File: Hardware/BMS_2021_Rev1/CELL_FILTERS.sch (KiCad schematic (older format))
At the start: 46 parts

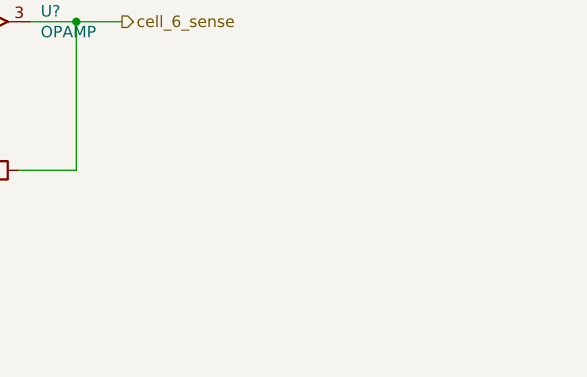
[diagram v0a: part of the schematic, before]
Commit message: TIVA added, current sense WIP
started the current sense circuit. added the tiva layout, need to ask if there is a better way
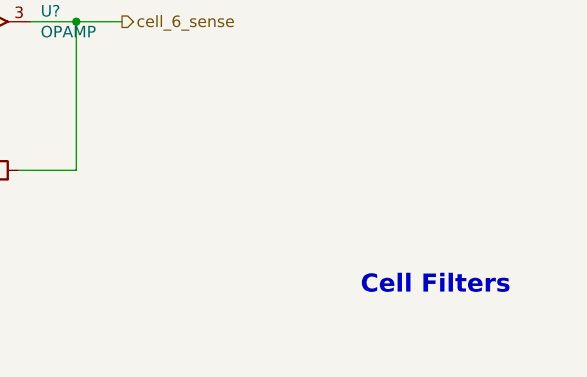
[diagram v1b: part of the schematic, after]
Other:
- note added: "Cell Filters"
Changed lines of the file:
@@
 $Descr USLetter 11000 8500
 encoding utf-8
-Sheet 3 3
+Sheet 3 4
 Title ""
 Date ""
@@
 Text Notes 7150 5550 0    50   Italic 10
 Questions: \nDiodes?\n
+Text Notes 7400 7750 2    79   ~ 16
+Cell Filters
 $EndSCHEMATC

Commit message: done (need to do LEDs)
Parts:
- removed R? (x13): R, symbol Device:R
- added R? (x13): 6.34M, symbol Device:R
- R?: value R -> 6.34M
- R?: value R -> 36.5k
- R?: value R -> 10k
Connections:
- net GND: now also R?.1, R?.1, R?.1, R?.1, R?.1, R?.1, R?.1
- net cell_3_sense: now also R?.1
- net cell_4_sense: now also R?.1
- net cell_5_sense: now also R?.1
- net cell_6_sense: now also R?.1
- net cell_7_sense: now also R?.1
- net cell_8_sense: now also R?.1
- net at R?.1, U?.1 (+): now also R?.2 (x6)
- net at R?.2, U?.2 (-): now also R?.2 (x5)
- net at R?.1, U?.2 (-): now also R?.2
- net at R?.2, U?.1 (+): now also R?.2
- net +5V renamed 5V

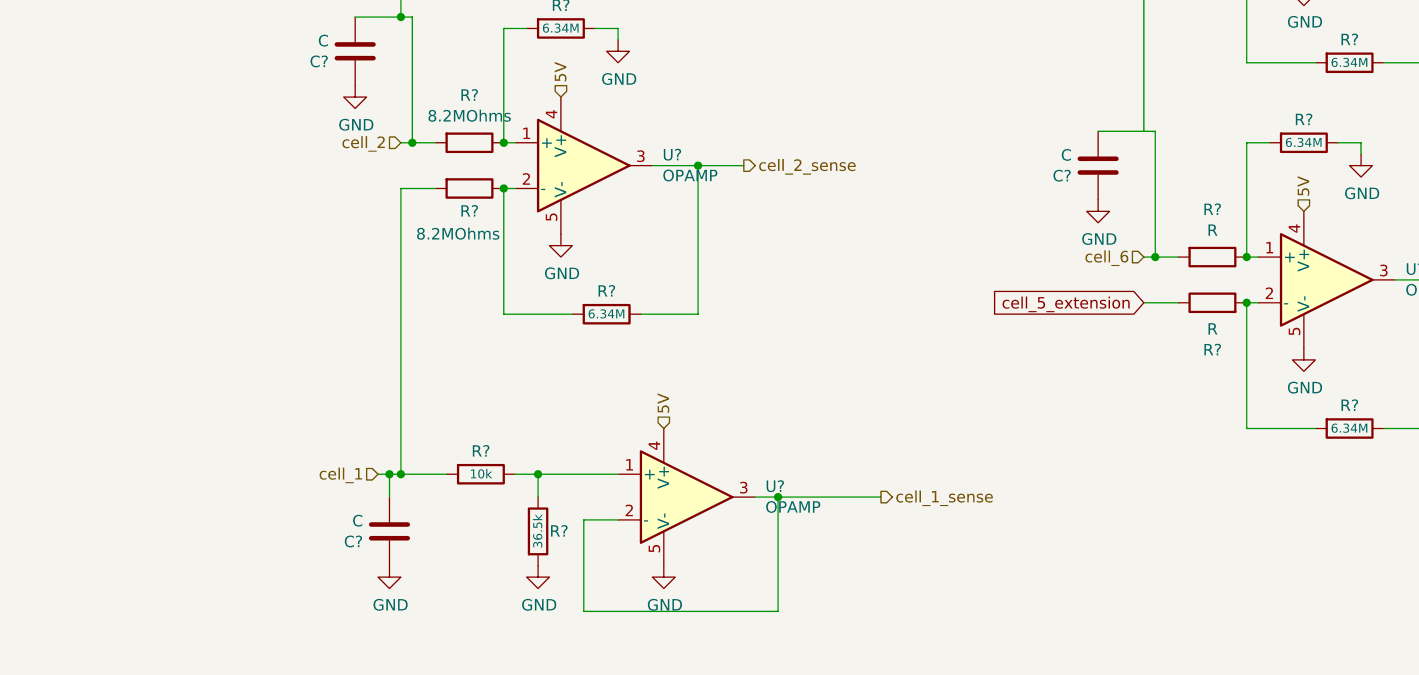
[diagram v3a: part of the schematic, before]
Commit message: notes from PDR made. to be fixed
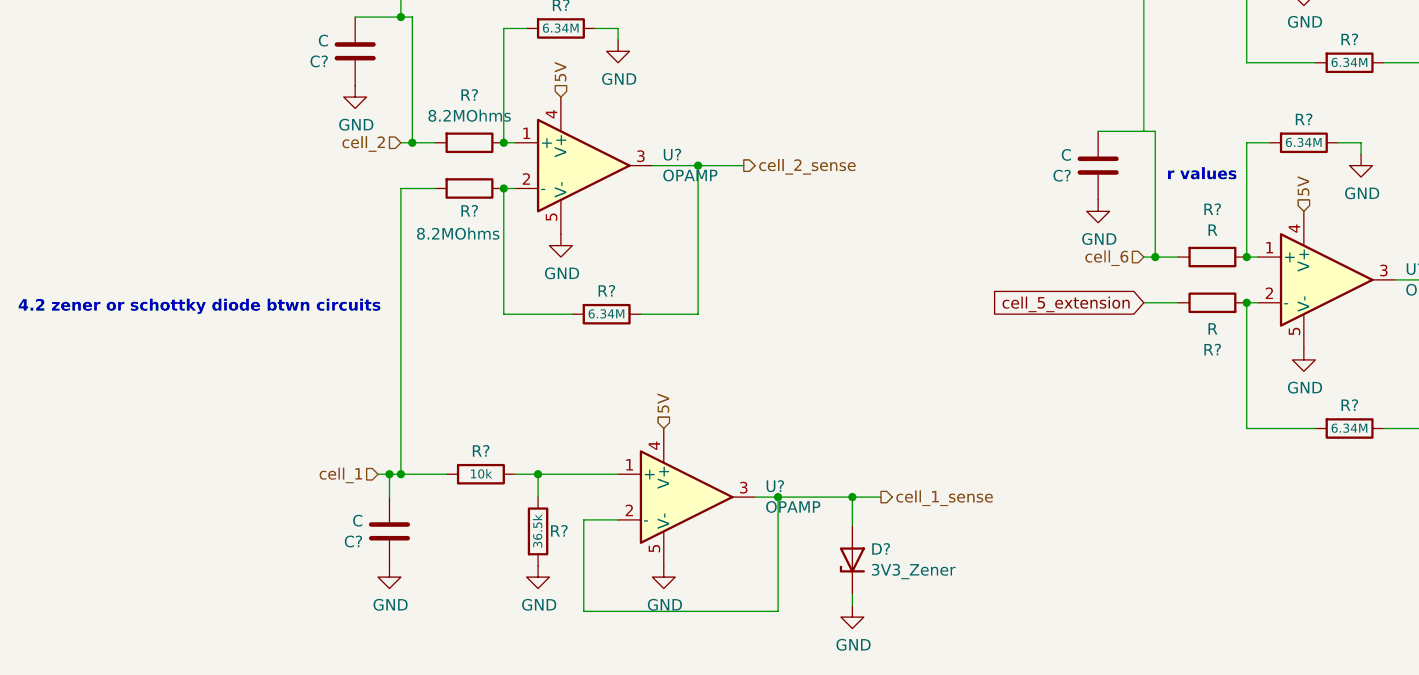
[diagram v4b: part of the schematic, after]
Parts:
- added D?: 3V3_Zener, symbol Device:D_Zener
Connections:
- net GND: now also D?.1 (K)
- net cell_1_sense: now also D?.2 (A)
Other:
- note added: "4.2 zener or schottky diode btwn circuits\n"
- note added: "r values"
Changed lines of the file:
@@
 	2600 7500 2500 7500
 Wire Wire Line
-	2600 7500 3050 7500
+	2600 7500 2925 7500
 Connection ~ 2600 7500
 $Comp
@@
 	0    1    1    0
 $EndComp
+$Comp
+L Device:D_Zener D?
+U 1 1 5F8CA6CA
+P 2925 7775
+F 0 "D?" V 2971 7695 50  0000 R CNN
+F 1 "3V3_Zener" V 2880 7695 50  0000 R CNN
+F 2 "" H 2925 7775 50  0001 C CNN
+F 3 "~" H 2925 7775 50  0001 C CNN
+	1    2925 7775
+	0    -1   -1   0
+$EndComp
+Wire Wire Line
+	2925 7625 2925 7500
+Connection ~ 2925 7500
+Wire Wire Line
+	2925 7500 3050 7500
+$Comp
+L power:GND #PWR?
+U 1 1 5F8D157C
+P 2925 7975
+F 0 "#PWR?" H 2925 7725 50  0001 C CNN
+F 1 "GND" H 2930 7802 50  0000 C CNN
+F 2 "" H 2925 7975 50  0001 C CNN
+F 3 "" H 2925 7975 50  0001 C CNN
+	1    2925 7975
+	1    0    0    -1
+$EndComp
+Wire Wire Line
+	2925 7975 2925 7925
+Text Notes -725 6700 0    50   ~ 10
+4.2 zener or schottky diode btwn circuits\n
+Text Notes 4300 6125 0    50   ~ 10
+r values
 $EndSCHEMATC

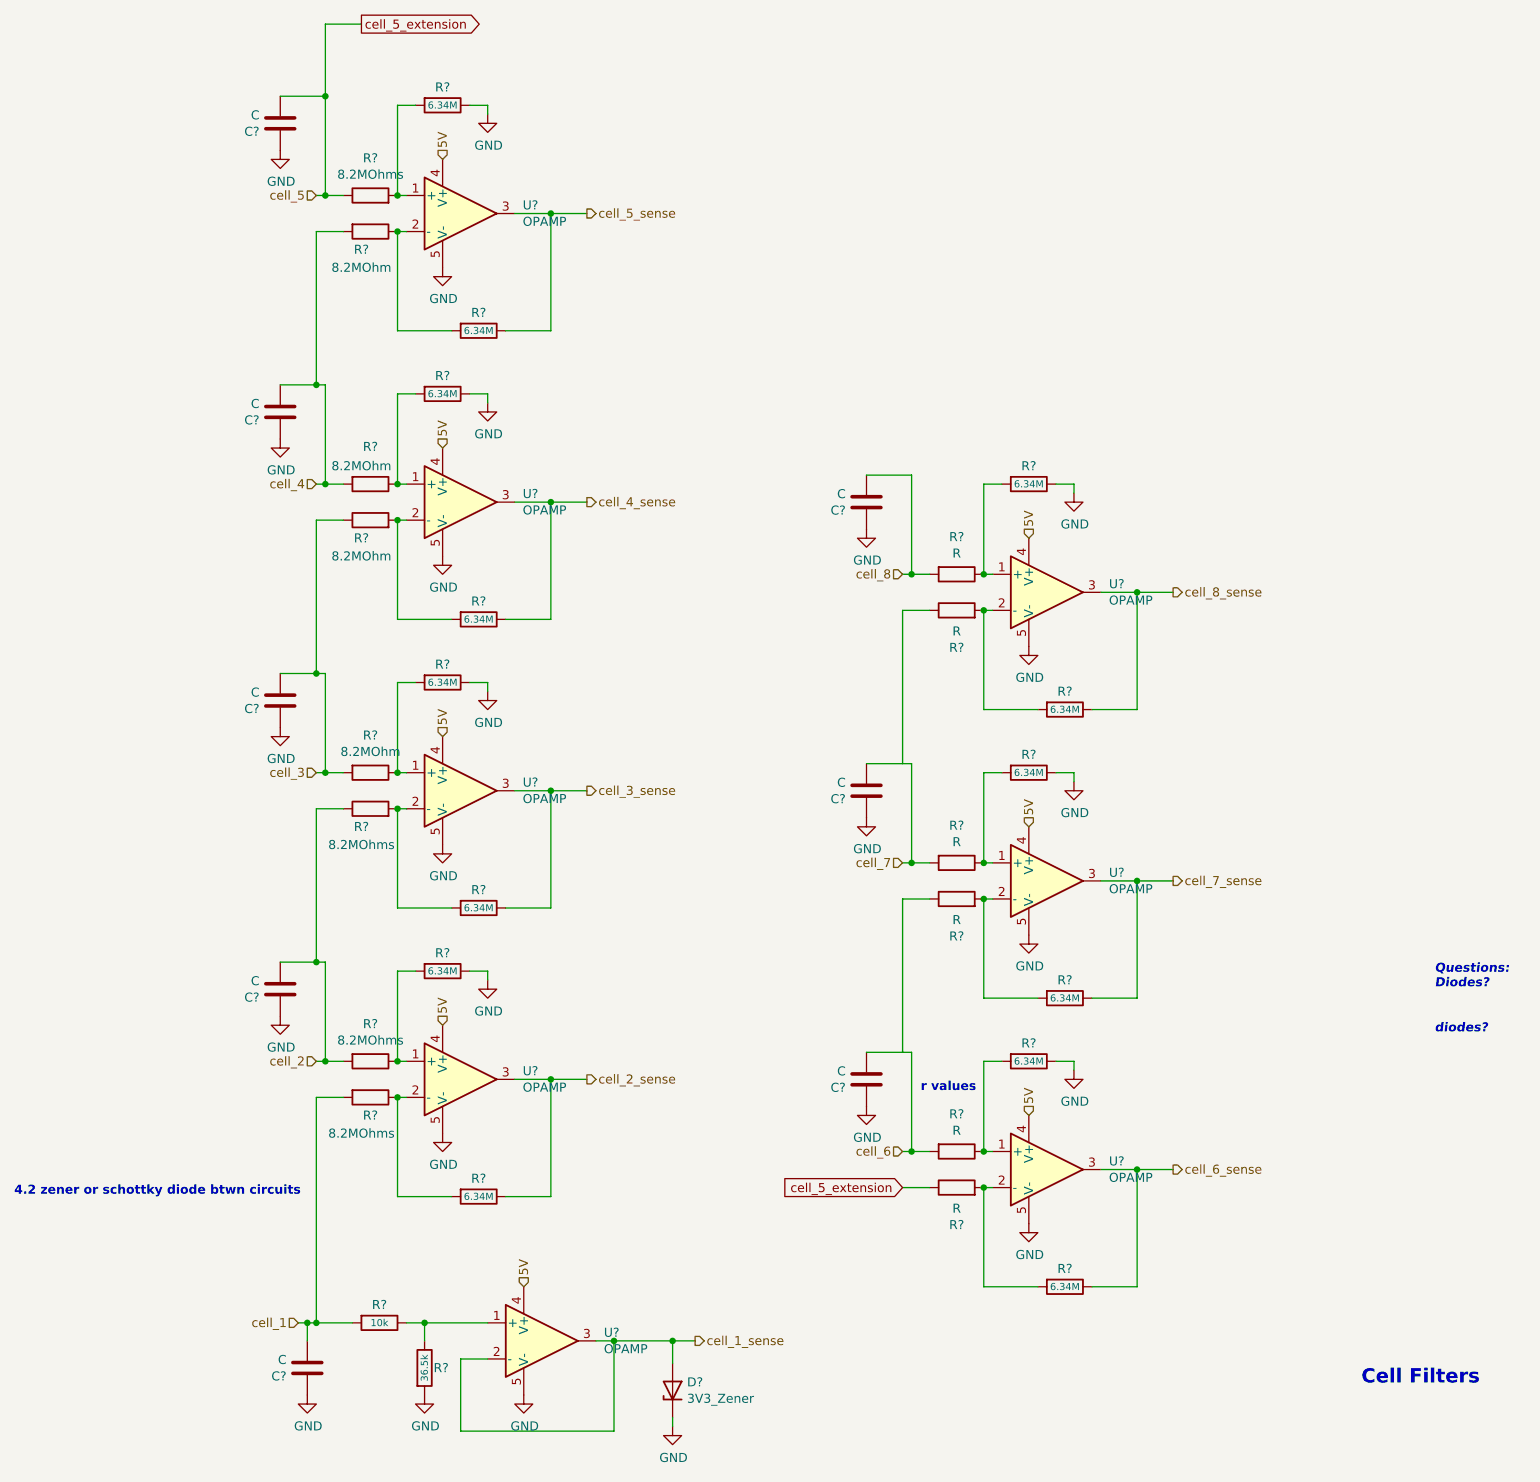
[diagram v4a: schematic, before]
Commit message: heirarchical sheets connected. Scho. diodes added to cell filters
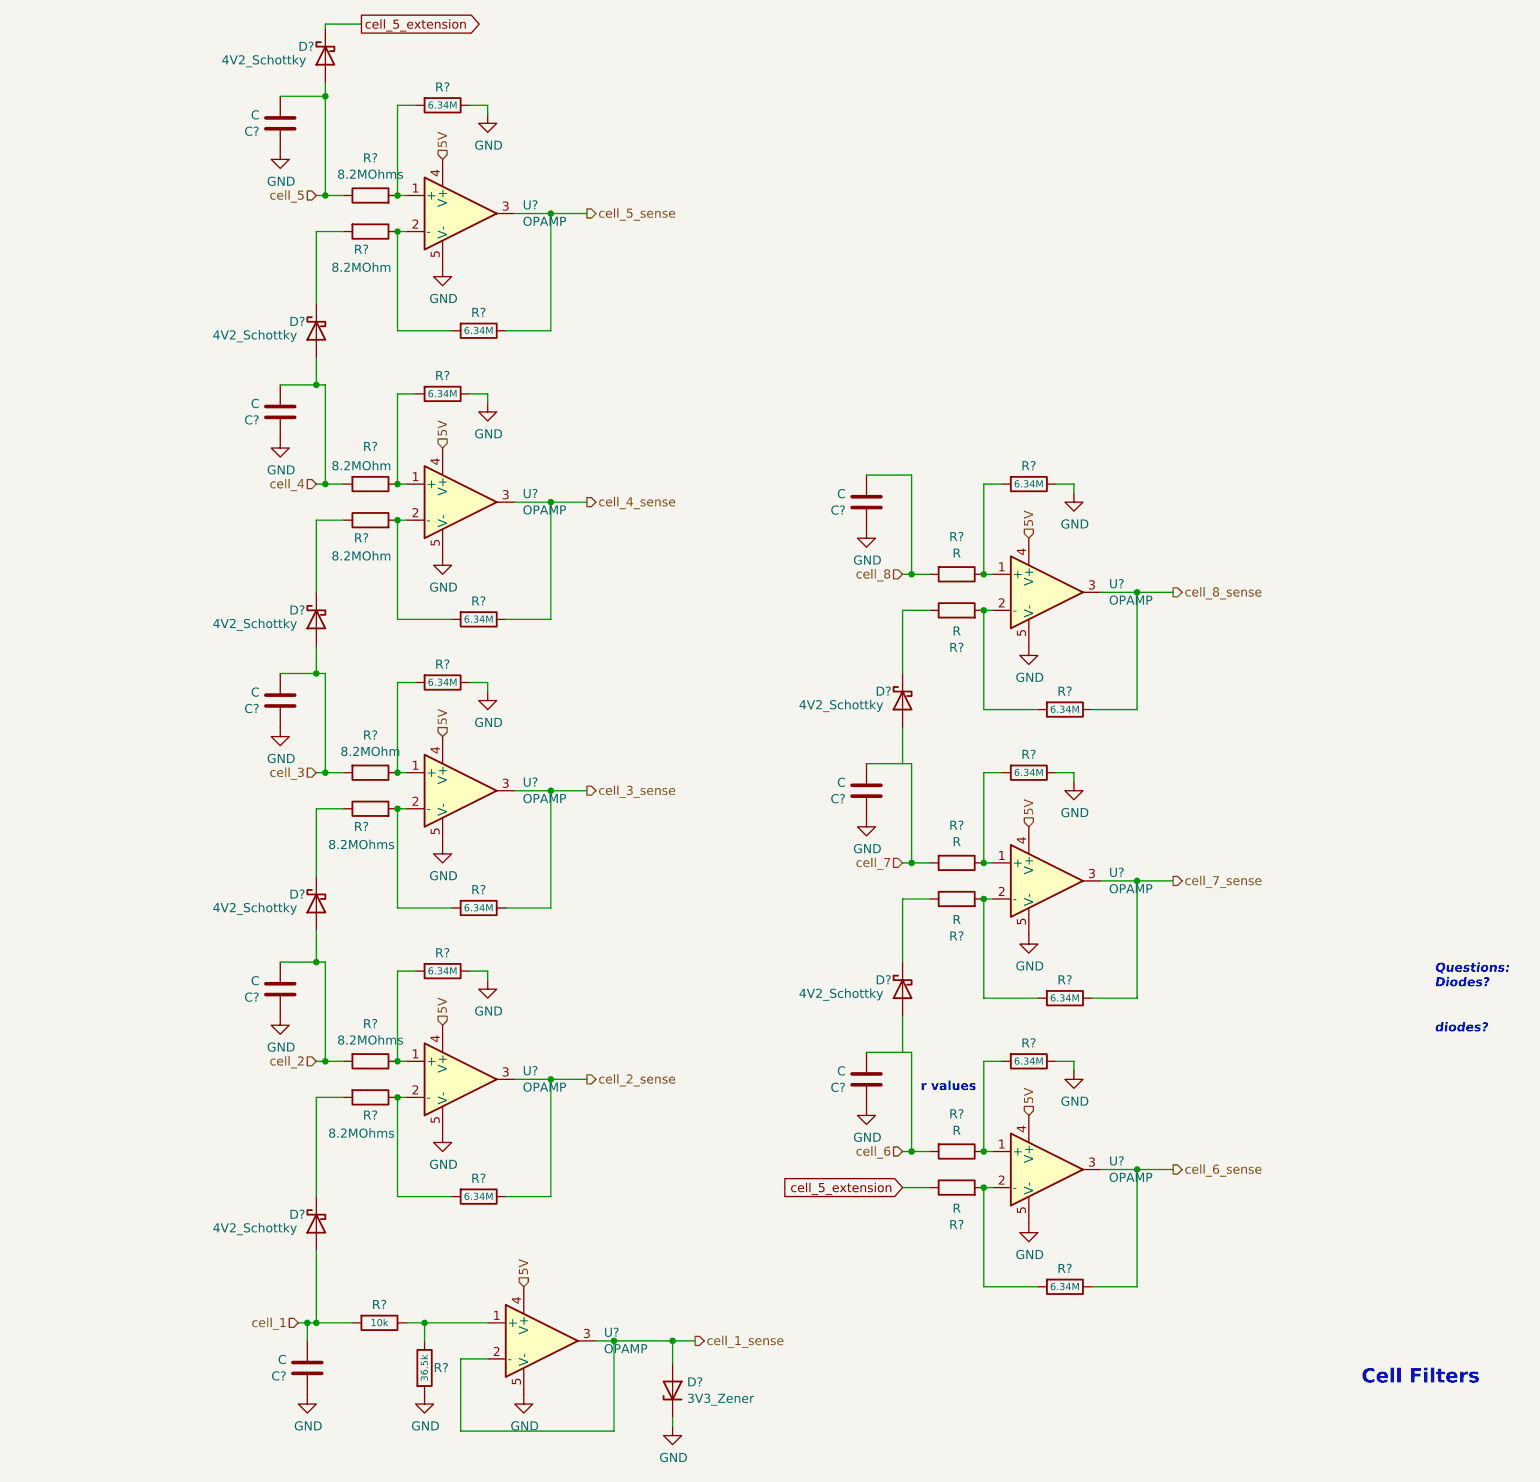
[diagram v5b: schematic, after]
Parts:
- added D? (x7): 4V2_Schottky, symbol Device:D_Schottky
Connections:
- net cell_1: now also D?.2 (A); no longer R?.2
- net cell_2: now also D?.2 (A); no longer R?.1
- net cell_3: now also D?.2 (A); no longer R?.1
- net cell_4: now also D?.2 (A); no longer R?.2
- net cell_5_extension: now also D?.1 (K); no longer C?.2, R?.1
- net at R?.1: now also D?.1 (K) (x2)
- new net: D?.1 (K), R?.2 (x2)
- new net: D?.1 (K), R?.1 (x2)
- new net cell_5: C?.2, D?.2 (A), R?.1
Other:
- note removed: "4.2 zener or schottky diode btwn circuits\n"
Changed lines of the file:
@@
 $Descr USLetter 11000 8500
 encoding utf-8
-Sheet 2 11
+Sheet 2 10
 Title ""
 Date ""
@@
 	950  4550 1100 4550
 Wire Wire Line
-	950  5400 950  4550
+	950  5400 950  5225
 $Comp
 L Device:R R?
@@
 	950  2950 1100 2950
 Wire Wire Line
-	950  3800 950  2950
+	950  3800 950  3650
 $Comp
 L Device:R R?
@@
 	950  1350 1100 1350
 Wire Wire Line
-	950  2200 950  1350
+	950  2200 950  2050
 $Comp
 L Device:R R?
@@
 Wire Wire Line
 	4200 5050 4350 5050
-Wire Wire Line
-	4200 5900 4200 5050
 $Comp
 L Device:R R?
@@
 Wire Wire Line
 	4200 3450 4350 3450
-Wire Wire Line
-	4200 4300 4200 3450
 $Comp
 L Device:R R?
@@
 $EndComp
 Wire Wire Line
-	950  7400 950  6150
+	950  7400 950  7000
 Wire Wire Line
 	950  6150 1100 6150
@@
 Wire Wire Line
 	750  600  1000 600
-Wire Wire Line
-	1000 600  1000 200
 Wire Wire Line
 	1000 200  1200 200
@@
 Wire Wire Line
 	2925 7975 2925 7925
-Text Notes -725 6700 0    50   ~ 10
-4.2 zener or schottky diode btwn circuits\n
 Text Notes 4300 6125 0    50   ~ 10
 r values
+$Comp
+L Device:D_Schottky D?
+U 1 1 5F94485A
+P 950 6850
+F 0 "D?" V 900 7000 50  0000 R CNN
+F 1 "4V2_Schottky" V 975 7425 50  0000 R CNN
+F 2 "" H 950 6850 50  0001 C CNN
+F 3 "~" H 950 6850 50  0001 C CNN
+	1    950  6850
+	0    -1   1    0
+$EndComp
+Wire Wire Line
+	950  6700 950  6150
+$Comp
+L Device:D_Schottky D?
+U 1 1 5F94E7ED
+P 950 5075
+F 0 "D?" V 900 5225 50  0000 R CNN
+F 1 "4V2_Schottky" V 975 5650 50  0000 R CNN
+F 2 "" H 950 5075 50  0001 C CNN
+F 3 "~" H 950 5075 50  0001 C CNN
+	1    950  5075
+	0    -1   1    0
+$EndComp
+$Comp
+L Device:D_Schottky D?
+U 1 1 5F954AC8
+P 950 3500
+F 0 "D?" V 900 3650 50  0000 R CNN
+F 1 "4V2_Schottky" V 975 4075 50  0000 R CNN
+F 2 "" H 950 3500 50  0001 C CNN
+F 3 "~" H 950 3500 50  0001 C CNN
+	1    950  3500
+	0    -1   1    0
+$EndComp
+$Comp
+L Device:D_Schottky D?
+U 1 1 5F95AE2A
+P 950 1900
+F 0 "D?" V 900 2050 50  0000 R CNN
+F 1 "4V2_Schottky" V 975 2475 50  0000 R CNN
+F 2 "" H 950 1900 50  0001 C CNN
+F 3 "~" H 950 1900 50  0001 C CNN
+	1    950  1900
+	0    -1   1    0
+$EndComp
+$Comp
+L Device:D_Schottky D?
+U 1 1 5F961402
+P 1000 375
+F 0 "D?" V 950 525 50  0000 R CNN
+F 1 "4V2_Schottky" V 1025 950 50  0000 R CNN
+F 2 "" H 1000 375 50  0001 C CNN
+F 3 "~" H 1000 375 50  0001 C CNN
+	1    1000 375
+	0    -1   1    0
+$EndComp
+Wire Wire Line
+	1000 200  1000 225
+Wire Wire Line
+	950  4925 950  4550
+Wire Wire Line
+	950  3350 950  2950
+Wire Wire Line
+	950  1750 950  1350
+Wire Wire Line
+	1000 525  1000 600
+$Comp
+L Device:D_Schottky D?
+U 1 1 5F96E38C
+P 4200 5550
+F 0 "D?" V 4150 5700 50  0000 R CNN
+F 1 "4V2_Schottky" V 4225 6125 50  0000 R CNN
+F 2 "" H 4200 5550 50  0001 C CNN
+F 3 "~" H 4200 5550 50  0001 C CNN
+	1    4200 5550
+	0    -1   1    0
+$EndComp
+Wire Wire Line
+	4200 5050 4200 5400
+Wire Wire Line
+	4200 5700 4200 5900
+$Comp
+L Device:D_Schottky D?
+U 1 1 5F97C0C8
+P 4200 3950
+F 0 "D?" V 4150 4100 50  0000 R CNN
+F 1 "4V2_Schottky" V 4225 4525 50  0000 R CNN
+F 2 "" H 4200 3950 50  0001 C CNN
+F 3 "~" H 4200 3950 50  0001 C CNN
+	1    4200 3950
+	0    -1   1    0
+$EndComp
+Wire Wire Line
+	4200 3450 4200 3800
+Wire Wire Line
+	4200 4100 4200 4300
 $EndSCHEMATC
